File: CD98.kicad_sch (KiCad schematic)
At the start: 213 parts, among them J1 Conn_01x20, J2 Conn_01x20, SW1 SW_Push, SW2 RotaryEncoder_Switch, U1 ATmega32U4-A, Y1 16MHz

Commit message: CD98 Keyboard v5
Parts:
- added F1: 500mA, symbol Device:Polyfuse_Small
- added USB1: Molex-0548190589, symbol random-keyboard-parts:Molex-0548190589
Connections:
- net +5V: now also F1.2
- net D+: now also USB1.3 (D+)
- net D-: now also USB1.4 (D-)
- net GND: now also USB1.1 (GND)
- new net VCC: F1.1, USB1.5 (VBUS)
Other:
- note added: "ADD USB-C"
- note removed: "ADD USB"

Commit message: v5
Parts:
- C1, C2, C3, C4, C5, C6, C7: footprint (none) -> Capacitor_SMD:C_0805_2012Metric
- D1, D10, D11, D12, D13, D14, D15, D16, D17, D18, D19, D2, D20, D21, D22, D23, D24, D25, D26, D27, D28, D29, D3, D30, D31, D32, D33, D34, D35, D36, D37, D38, D39, D4, D40, D41, D42, D43, D44, D45, D46, D47, D48, D49, D5, D50, D51, D52, D53, D54, D55, D56, D57, D58, D59, D6, D60, D61, D62, D63, D64, D65, D66, D67, D68, D69, D7, D70, D71, D72, D73, D74, D75, D76, D77, D78, D79, D8, D80, D81, D82, D83, D84, D85, D86, D87, D88, D89, D9, D90, D91, D92, D93, D94, D95, D96, D97, D98: footprint (none) -> Diode_SMD:D_SOD-123
- F1: footprint (none) -> Fuse:Fuse_1206_3216Metric
- J1, J2: footprint (none) -> Connector_PinSocket_2.54mm:PinSocket_1x20_P2.54mm_Horizontal
- MX1, MX10, MX11, MX12, MX13, MX14, MX15, MX16, MX17, MX18, MX19, MX2, MX20, MX21, MX22, MX23, MX24, MX25, MX26, MX27, MX28, MX29, MX3, MX30, MX31, MX32, MX33, MX34, MX35, MX36, MX37, MX38, MX39, MX4, MX40, MX41, MX42, MX43, MX44, MX45, MX46, MX47, MX48, MX49, MX5, MX50, MX51, MX52, MX53, MX54, MX55, MX56, MX57, MX58, MX59, MX6, MX60, MX61, MX62, MX63, MX64, MX65, MX66, MX67, MX68, MX69, MX7, MX70, MX71, MX72, MX73, MX74, MX75, MX76, MX77, MX78, MX79, MX8, MX80, MX81, MX82, MX83, MX84, MX85, MX86, MX87, MX88, MX89, MX9, MX90, MX91, MX92, MX93, MX94, MX95, MX96, MX97, MX98: footprint (none) -> MX_Only:MXOnly-1U-Hotswap
- R1, R2: footprint (none) -> Resistor_SMD:R_0805_2012Metric
- Rd1: renamed from Rd; footprint (none) -> Resistor_SMD:R_0805_2012Metric
- Rr1: renamed from Rr; footprint (none) -> Resistor_SMD:R_0805_2012Metric
- SW1: footprint (none) -> random-keyboard-parts:SKQG-1155865
- SW2: footprint (none) -> Rotary_Encoder:RotaryEncoder_Alps_EC12E-Switch_Vertical_H20mm
- USB1: footprint (none) -> random-keyboard-parts:Molex-0548190589
- Y1: footprint (none) -> Crystal:Crystal_SMD_3225-4Pin_3.2x2.5mm_HandSoldering
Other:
- note added: "-ADD USB-C"
- note removed: "ADD USB-C"

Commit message: v5
Remapped error from previous schematic, positioned key switches in pcb.
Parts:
- MX30: footprint MX_Only:MXOnly-1U-Hotswap -> MX_Only:MXOnly-2U-Hotswap
- MX32: footprint MX_Only:MXOnly-1U-Hotswap -> MX_Only:MXOnly-1.5U-Hotswap
- MX45: footprint MX_Only:MXOnly-1U-Hotswap -> MX_Only:MXOnly-ISO-Hotswap
- MX47, MX72: footprint MX_Only:MXOnly-1U-Hotswap -> MX_Only:MXOnly-1.75U-Hotswap
- MX61: footprint MX_Only:MXOnly-1U-Hotswap -> MX_Only:MXOnly-2.25U-Hotswap
- MX75, MX76, MX77: footprint MX_Only:MXOnly-1U-Hotswap -> MX_Only:MXOnly-1.25U-Hotswap
- MX78: footprint MX_Only:MXOnly-1U-Hotswap -> MX_Only:MXOnly-6.25U-Hotswap
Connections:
- net Col 0: no longer J1.1 (Pin_1), MX1.1 (COL), MX17.1 (COL), MX32.1 (COL), MX47.1 (COL), MX77.1 (COL)
- net Col 1: no longer J1.2 (Pin_2), MX18.1 (COL), MX2.1 (COL), MX61.1 (COL), MX78.1 (COL)
- net Col 3: no longer J1.4 (Pin_4), MX20.1 (COL), MX34.1 (COL), MX4.1 (COL), MX49.1 (COL), MX63.1 (COL), MX75.1 (COL)
- net Col 6: no longer J1.7 (Pin_7), MX23.1 (COL), MX37.1 (COL), MX52.1 (COL), MX66.1 (COL), MX7.1 (COL), MX76.1 (COL)
- new net: J1.2 (Pin_2), MX18.1 (COL), MX2.1 (COL), MX61.1 (COL), MX76.1 (COL)
- new net: J1.7 (Pin_7), MX23.1 (COL), MX37.1 (COL), MX52.1 (COL), MX66.1 (COL), MX7.1 (COL), MX78.1 (COL)
- new net: J1.1 (Pin_1), MX1.1 (COL), MX17.1 (COL), MX32.1 (COL), MX47.1 (COL), MX75.1 (COL)
- new net: J1.4 (Pin_4), MX20.1 (COL), MX34.1 (COL), MX4.1 (COL), MX49.1 (COL), MX63.1 (COL), MX77.1 (COL)
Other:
- moved on the sheet: D75, D76, D77, D78, MX75, MX76, MX77, MX78

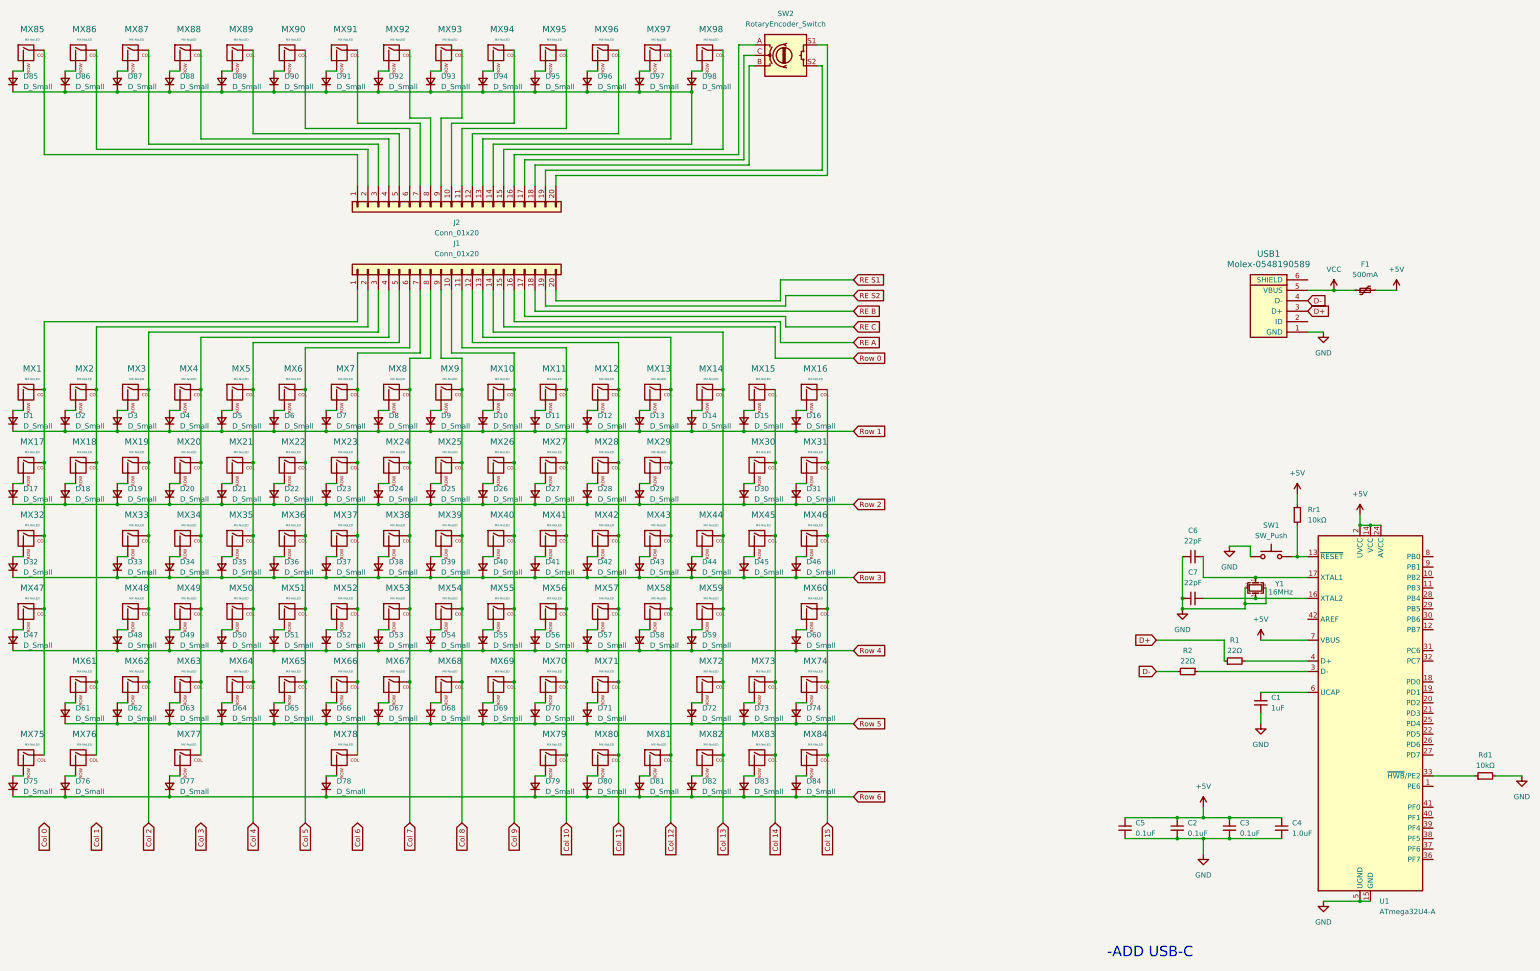
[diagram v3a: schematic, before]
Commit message: v5
Repositioned diodes, wired matrix.
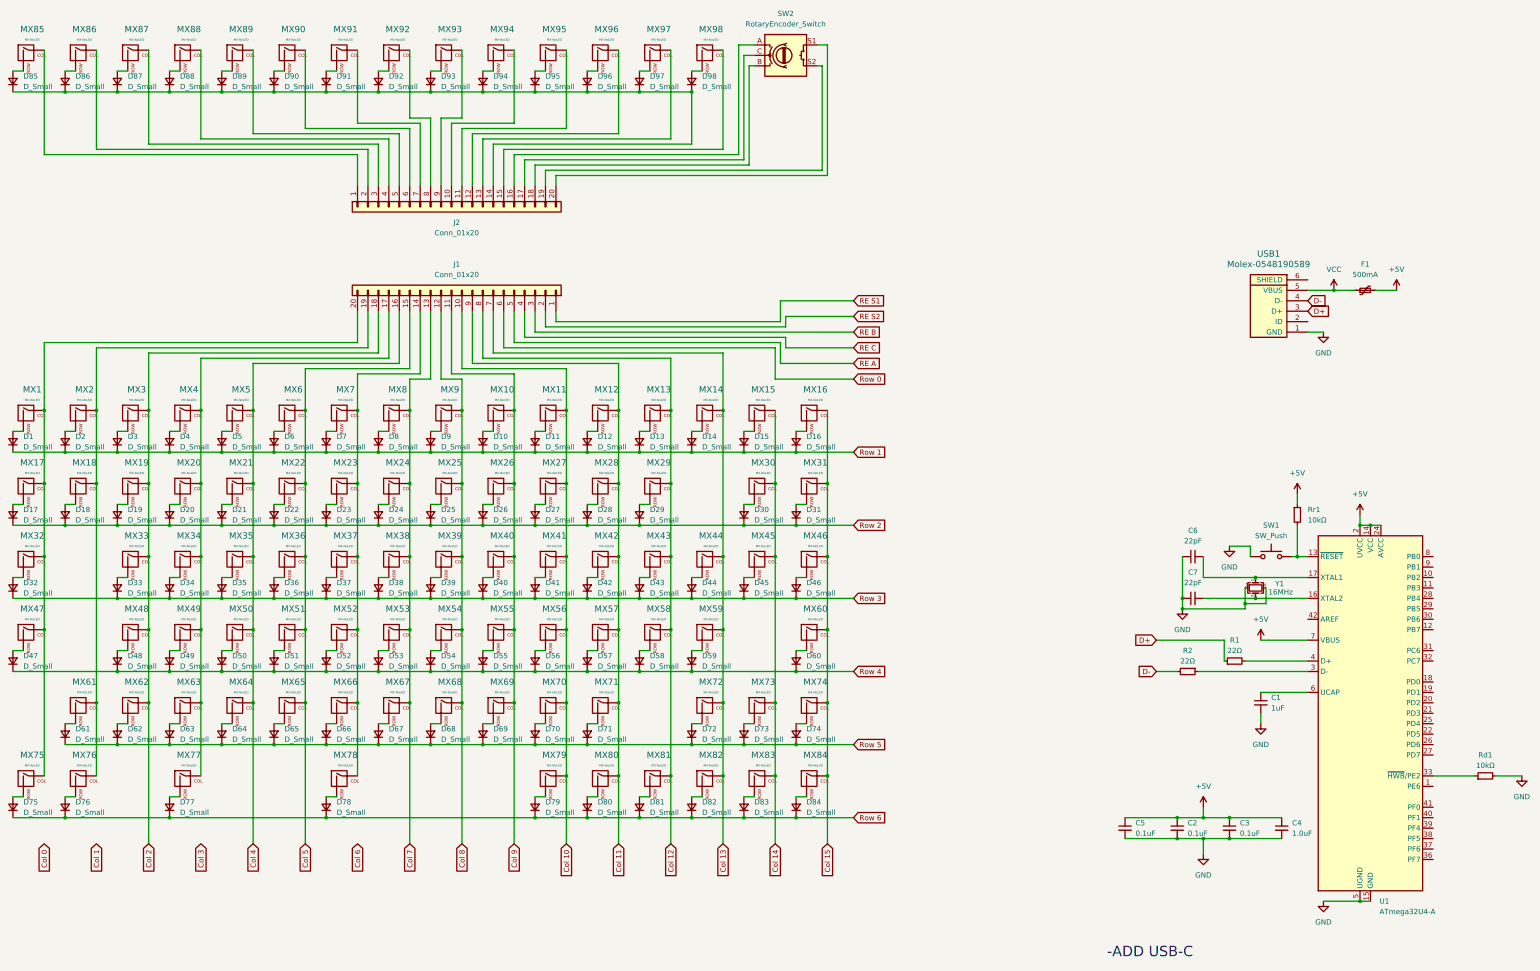
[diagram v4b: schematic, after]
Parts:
- J1, J2: footprint Connector_PinSocket_2.54mm:PinSocket_1x20_P2.54mm_Horizontal -> Connector_PinSocket_2.00mm:PinSocket_1x20_P2.00mm_Horizontal
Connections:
- net Col 10: now also J1.10 (Pin_10); no longer J1.11 (Pin_11)
- net Col 11: now also J1.9 (Pin_9); no longer J1.12 (Pin_12)
- net Col 12: now also J1.8 (Pin_8); no longer J1.13 (Pin_13)
- net Col 13: now also J1.7 (Pin_7); no longer J1.14 (Pin_14)
- net Col 2: now also J1.18 (Pin_18); no longer J1.3 (Pin_3)
- net Col 4: now also J1.16 (Pin_16); no longer J1.5 (Pin_5)
- net Col 5: now also J1.15 (Pin_15); no longer J1.6 (Pin_6)
- net Col 7: now also J1.13 (Pin_13); no longer J1.8 (Pin_8)
- net Col 8: now also J1.12 (Pin_12); no longer J1.9 (Pin_9)
- net Col 9: now also J1.11 (Pin_11); no longer J1.10 (Pin_10)
- net RE A: now also J1.5 (Pin_5); no longer J1.16 (Pin_16)
- net RE B: now also J1.3 (Pin_3); no longer J1.18 (Pin_18)
- net RE C: now also J1.4 (Pin_4); no longer J1.17 (Pin_17)
- net RE S1: now also J1.1 (Pin_1); no longer J1.20 (Pin_20)
- net RE S2: now also J1.2 (Pin_2); no longer J1.19 (Pin_19)
- net Row 0: now also J1.6 (Pin_6); no longer J1.15 (Pin_15)
- net at MX18.1 (COL), MX2.1 (COL), MX61.1 (COL)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: now also J1.19 (Pin_19); no longer J1.2 (Pin_2)
- net at MX23.1 (COL), MX37.1 (COL), MX52.1 (COL)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: now also J1.14 (Pin_14); no longer J1.7 (Pin_7)
- net at MX1.1 (COL), MX17.1 (COL), MX32.1 (COL)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: now also J1.20 (Pin_20); no longer J1.1 (Pin_1)
- net at MX20.1 (COL), MX34.1 (COL), MX4.1 (COL)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: now also J1.17 (Pin_17); no longer J1.4 (Pin_4)
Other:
- moved on the sheet: D1, D10, D11, D12, D13, D14, D15, D16, D17, D18, D19, D2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
